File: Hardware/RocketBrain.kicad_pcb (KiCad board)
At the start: 4 copper layers, 52 x 24 mm, 59 parts, among them J1 Screw_Terminal_01x02, J2 1x3 picoblade, J3 1x3 picoblade, J4 1x2 picoblade, J5 DM3CS-SF, J6 Screw_Terminal_01x02, J7 Screw_Terminal_01x02, Q1 G1003A, Q2 G1003A, U1 Pico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

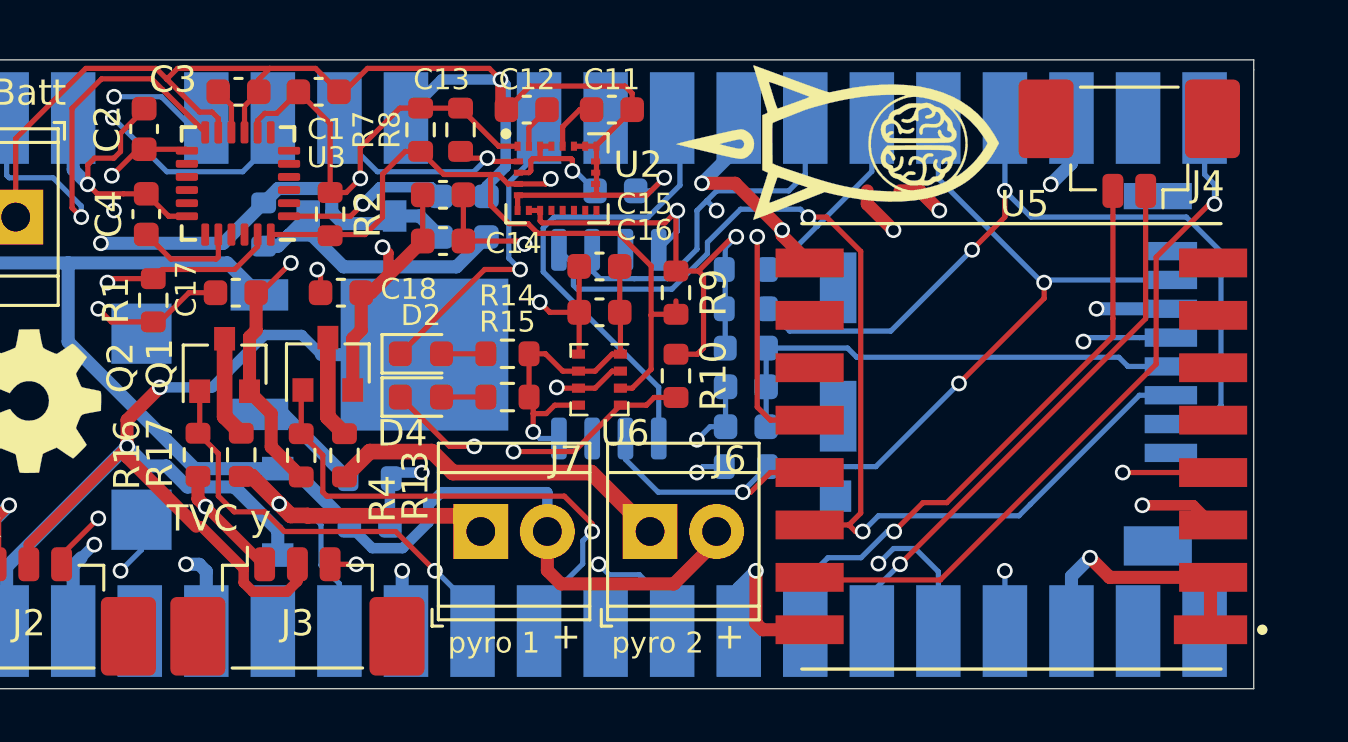
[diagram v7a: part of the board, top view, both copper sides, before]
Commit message: Widen board, reposition LoRa capacitors
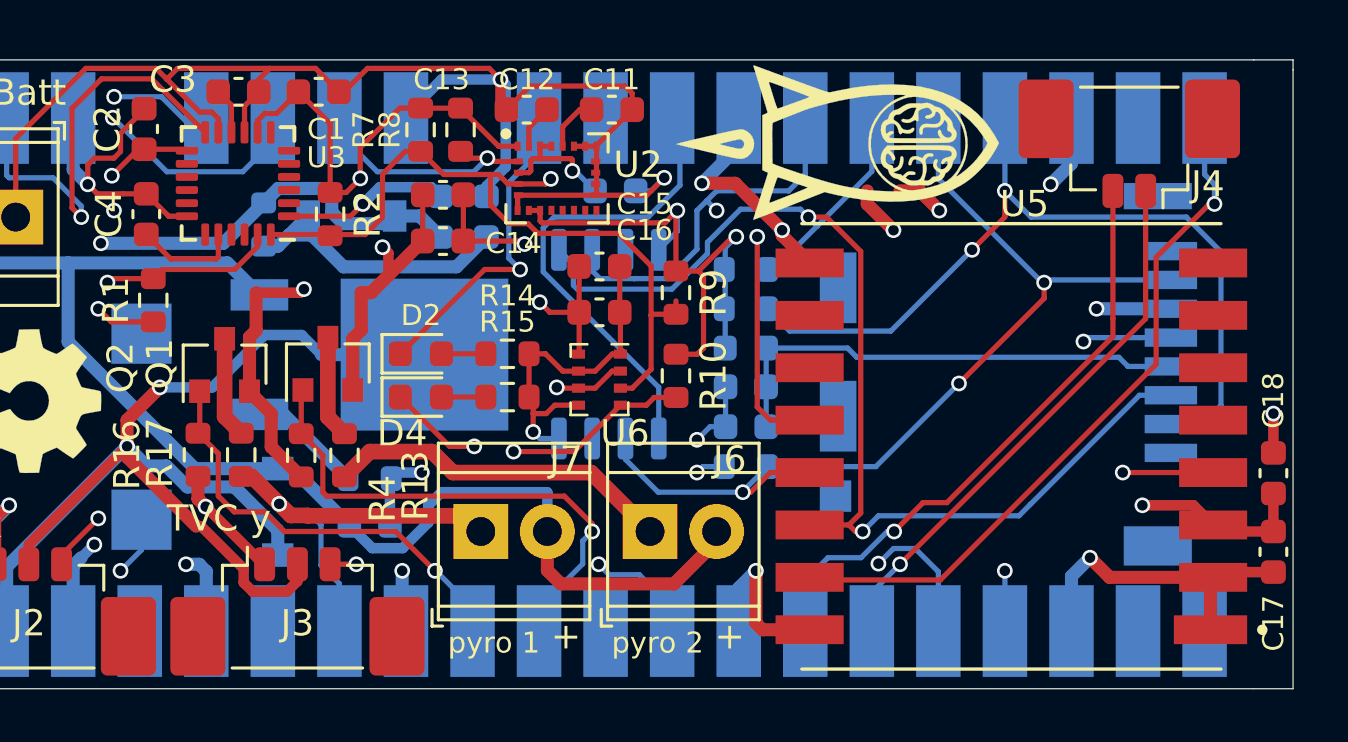
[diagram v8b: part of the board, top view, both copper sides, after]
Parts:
- moved C17 40.8 mm to (165.5, 82.8), turned to 270 degrees
- moved C18 36.3 mm to (165.5, 79.8), turned to 90 degrees
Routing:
- net GND: track 165.8 -> 169.7 mm, vias 20 -> 21
- net +3V3: track 116.0 -> 116.3 mm, vias 13 -> 12
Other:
- board size 52 x 24 mm -> 53.5 x 24 mm
